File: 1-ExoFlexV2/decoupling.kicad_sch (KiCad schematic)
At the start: 158 parts

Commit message: Schématisation terminée
- Schéma terminé
- Passage vers le PCB
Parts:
- C100, C101, C110, C111, C112, C113, C114, C115, C116, C117, C125, C126, C127, C128, C129, C130, C131, C139, C140, C141, C142, C143, C144, C145, C153, C154, C155, C156, C157, C158, C159, C62, C63, C64, C65, C66, C67, C68, C69, C78, C79, C80, C81, C82, C83, C84, C85, C94, C95, C96, C97, C98, C99: renamed from C?; value 1uF -> 1uF 10V X6S; footprint Capacitor_SMD:C_0603_1608Metric -> Capacitor_SMD:C_0402_1005Metric; DESCRIPTION (none) -> 1 µF ±10% 10V Ceramic Capacitor X6S 0402 (1005 Metric); MANUFACTURER (none) -> Murata Electronics; PACKAGE (none) -> 0402 (1005 Metric); PART NUMBER (none) -> GRM155C81A105KA12D; TYPE (none) -> SMD
- C102, C103, C104, C105, C106, C107, C108, C109, C118, C119, C120, C121, C122, C123, C124, C132, C133, C134, C135, C136, C137, C138, C146, C147, C148, C149, C150, C151, C152, C160, C161, C162, C164, C165, C166, C167, C168, C169, C170, C171, C172, C173, C174, C175, C176, C177, C178, C179, C180, C181, C182, C183, C184, C185, C186, C187, C188, C189, C190, C191, C192, C193, C194, C195, C196, C197, C198, C199, C200, C201, C202, C203, C204, C205, C206, C207, C208, C209, C210, C211, C54, C55, C56, C57, C58, C59, C60, C61, C70, C71, C72, C73, C74, C75, C76, C77, C86, C87, C88, C89, C90, C91, C92, C93: renamed from C?; value 0,1uF -> 0,1uF 10V X5R; footprint Capacitor_SMD:C_0603_1608Metric -> Capacitor_SMD:C_0402_1005Metric; DESCRIPTION (none) -> 0.1 µF ±10% 10V Ceramic Capacitor X5R 0402 (1005 Metric); MANUFACTURER (none) -> Murata Electronics; PACKAGE (none) -> 0402 (1005 Metric); PART NUMBER (none) -> GRM155R61A104KA01D; TYPE (none) -> SMD
- C163: renamed from C?; value 0,1uF -> 0,1uF 10V X5R; footprint FootPrintLib:CAPC220145_88N_KEM -> Capacitor_SMD:C_0402_1005Metric; DESCRIPTION (none) -> 0.1 µF ±10% 10V Ceramic Capacitor X5R 0402 (1005 Metric); MANUFACTURER (none) -> Murata Electronics; PACKAGE (none) -> 0402 (1005 Metric); PART NUMBER (none) -> GRM155R61A104KA01D; TYPE (none) -> SMD

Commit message: PLACEMENT 1
- Placement des connnecteurs
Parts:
- added H1: MH1, MountingHole:MountingHole_2.2mm_M2, symbol Mechanical:MountingHole
- added H2: MH2, MountingHole:MountingHole_2.2mm_M2, symbol Mechanical:MountingHole
- added H3: MH3, MountingHole:MountingHole_2.2mm_M2, symbol Mechanical:MountingHole
- added H4: MH4, MountingHole:MountingHole_2.2mm_M2, symbol Mechanical:MountingHole
- added H5: MH5, MountingHole:MountingHole_2.2mm_M2, symbol Mechanical:MountingHole
- added H6: MH6, MountingHole:MountingHole_2.2mm_M2, symbol Mechanical:MountingHole
- added H7: MH7, MountingHole:MountingHole_2.2mm_M2, symbol Mechanical:MountingHole
- added H8: MH8, MountingHole:MountingHole_2.2mm_M2, symbol Mechanical:MountingHole
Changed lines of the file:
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@@
     (pin "2")
   )
+  (symbol (lib_id "Mechanical:MountingHole") (at 93.98 181.61 0) (unit 1)
+    (in_bom yes) (on_board yes)
+    (property "Reference" "H4" (id 0) (at 96.52 180.3399 0)
+      (effects (font (size 1.27 1.27)) (justify left))
+    )
+    (property "Value" "MH4" (id 1) (at 91.44 184.15 0)
+      (effects (font (size 1.27 1.27)) (justify left))
+    )
+    (property "Footprint" "MountingHole:MountingHole_2.2mm_M2" (id 2) (at 93.98 181.61 0)
+      (effects (font (size 1.27 1.27)) hide)
+    )
+    (property "Datasheet" "~" (id 3) (at 93.98 181.61 0)
+      (effects (font (size 1.27 1.27)) hide)
+    )
+  )
   (symbol (lib_id "Device:C") (at 214.63 132.08 0) (unit 1)
     (in_bom yes) (on_board yes)
@@
     (pin "2")
   )
+  (symbol (lib_id "Mechanical:MountingHole") (at 76.2 181.61 0) (unit 1)
+    (in_bom yes) (on_board yes)
+    (property "Reference" "H2" (id 0) (at 78.74 180.3399 0)
+      (effects (font (size 1.27 1.27)) (justify left))
+    )
+    (property "Value" "MH2" (id 1) (at 73.66 184.15 0)
+      (effects (font (size 1.27 1.27)) (justify left))
+    )
+    (property "Footprint" "MountingHole:MountingHole_2.2mm_M2" (id 2) (at 76.2 181.61 0)
+      (effects (font (size 1.27 1.27)) hide)
+    )
+    (property "Datasheet" "~" (id 3) (at 76.2 181.61 0)
+      (effects (font (size 1.27 1.27)) hide)
+    )
+  )
   (symbol (lib_id "Device:C") (at 223.52 54.61 0) (unit 1)
     (in_bom yes) (on_board yes)
@@
     (pin "2")
   )
+  (symbol (lib_id "Mechanical:MountingHole") (at 85.09 181.61 0) (unit 1)
+    (in_bom yes) (on_board yes)
+    (property "Reference" "H3" (id 0) (at 87.63 180.3399 0)
+      (effects (font (size 1.27 1.27)) (justify left))
+    )
+    (property "Value" "MH3" (id 1) (at 82.55 184.15 0)
+      (effects (font (size 1.27 1.27)) (justify left))
+    )
+    (property "Footprint" "MountingHole:MountingHole_2.2mm_M2" (id 2) (at 85.09 181.61 0)
+      (effects (font (size 1.27 1.27)) hide)
+    )
+    (property "Datasheet" "~" (id 3) (at 85.09 181.61 0)
+      (effects (font (size 1.27 1.27)) hide)
+    )
+  )
   (symbol (lib_id "Device:C") (at 259.08 54.61 0) (unit 1)
     (in_bom yes) (on_board yes)
@@
     (pin "2")
   )
+  (symbol (lib_id "Mechanical:MountingHole") (at 102.87 181.61 0) (unit 1)
+    (in_bom yes) (on_board yes)
+    (property "Reference" "H5" (id 0) (at 105.41 180.3399 0)
+      (effects (font (size 1.27 1.27)) (justify left))
+    )
+    (property "Value" "MH5" (id 1) (at 100.33 184.15 0)
+      (effects (font (size 1.27 1.27)) (justify left))
+    )
+    (property "Footprint" "MountingHole:MountingHole_2.2mm_M2" (id 2) (at 102.87 181.61 0)
+      (effects (font (size 1.27 1.27)) hide)
+    )
+    (property "Datasheet" "~" (id 3) (at 102.87 181.61 0)
+      (effects (font (size 1.27 1.27)) hide)
+    )
+  )
   (symbol (lib_id "Device:C") (at 86.36 55.88 0) (unit 1)
     (in_bom yes) (on_board yes)
@@
     (pin "2")
   )
+  (symbol (lib_id "Mechanical:MountingHole") (at 67.31 181.61 0) (unit 1)
+    (in_bom yes) (on_board yes)
+    (property "Reference" "H1" (id 0) (at 69.85 180.3399 0)
+      (effects (font (size 1.27 1.27)) (justify left))
+    )
+    (property "Value" "MH1" (id 1) (at 64.77 184.15 0)
+      (effects (font (size 1.27 1.27)) (justify left))
+    )
+    (property "Footprint" "MountingHole:MountingHole_2.2mm_M2" (id 2) (at 67.31 181.61 0)
+      (effects (font (size 1.27 1.27)) hide)
+    )
+    (property "Datasheet" "~" (id 3) (at 67.31 181.61 0)
+      (effects (font (size 1.27 1.27)) hide)
+    )
+  )
   (symbol (lib_id "Device:C") (at 147.32 41.91 0) (unit 1)
     (in_bom yes) (on_board yes)
@@
     (pin "2")
   )
+  (symbol (lib_id "Mechanical:MountingHole") (at 129.54 181.61 0) (unit 1)
+    (in_bom yes) (on_board yes)
+    (property "Reference" "H8" (id 0) (at 132.08 180.3399 0)
+      (effects (font (size 1.27 1.27)) (justify left))
+    )
+    (property "Value" "MH8" (id 1) (at 127 184.15 0)
+      (effects (font (size 1.27 1.27)) (justify left))
+    )
+    (property "Footprint" "MountingHole:MountingHole_2.2mm_M2" (id 2) (at 129.54 181.61 0)
+      (effects (font (size 1.27 1.27)) hide)
+    )
+    (property "Datasheet" "~" (id 3) (at 129.54 181.61 0)
+      (effects (font (size 1.27 1.27)) hide)
+    )
+  )
   (symbol (lib_id "Device:C") (at 250.19 67.31 0) (unit 1)
     (in_bom yes) (on_board yes)
@@
     (pin "2")
   )
+  (symbol (lib_id "Mechanical:MountingHole") (at 120.65 181.61 0) (unit 1)
+    (in_bom yes) (on_board yes)
+    (property "Reference" "H7" (id 0) (at 123.19 180.3399 0)
+      (effects (font (size 1.27 1.27)) (justify left))
+    )
+    (property "Value" "MH7" (id 1) (at 118.11 184.15 0)
+      (effects (font (size 1.27 1.27)) (justify left))
+    )
+    (property "Footprint" "MountingHole:MountingHole_2.2mm_M2" (id 2) (at 120.65 181.61 0)
+      (effects (font (size 1.27 1.27)) hide)
+    )
+    (property "Datasheet" "~" (id 3) (at 120.65 181.61 0)
+      (effects (font (size 1.27 1.27)) hide)
+    )
+  )
   (symbol (lib_id "Device:C") (at 50.8 133.35 0) (unit 1)
     (in_bom yes) (on_board yes)
@@
     (pin "2")
   )
+  (symbol (lib_id "Mechanical:MountingHole") (at 111.76 181.61 0) (unit 1)
+    (in_bom yes) (on_board yes)
+    (property "Reference" "H6" (id 0) (at 114.3 180.3399 0)
+      (effects (font (size 1.27 1.27)) (justify left))
+    )
+    (property "Value" "MH6" (id 1) (at 109.22 184.15 0)
+      (effects (font (size 1.27 1.27)) (justify left))
+    )
+    (property "Footprint" "MountingHole:MountingHole_2.2mm_M2" (id 2) (at 111.76 181.61 0)
+      (effects (font (size 1.27 1.27)) hide)
+    )
+    (property "Datasheet" "~" (id 3) (at 111.76 181.61 0)
+      (effects (font (size 1.27 1.27)) hide)
+    )
+  )
   (symbol (lib_id "Device:C") (at 187.96 93.98 0) (unit 1)

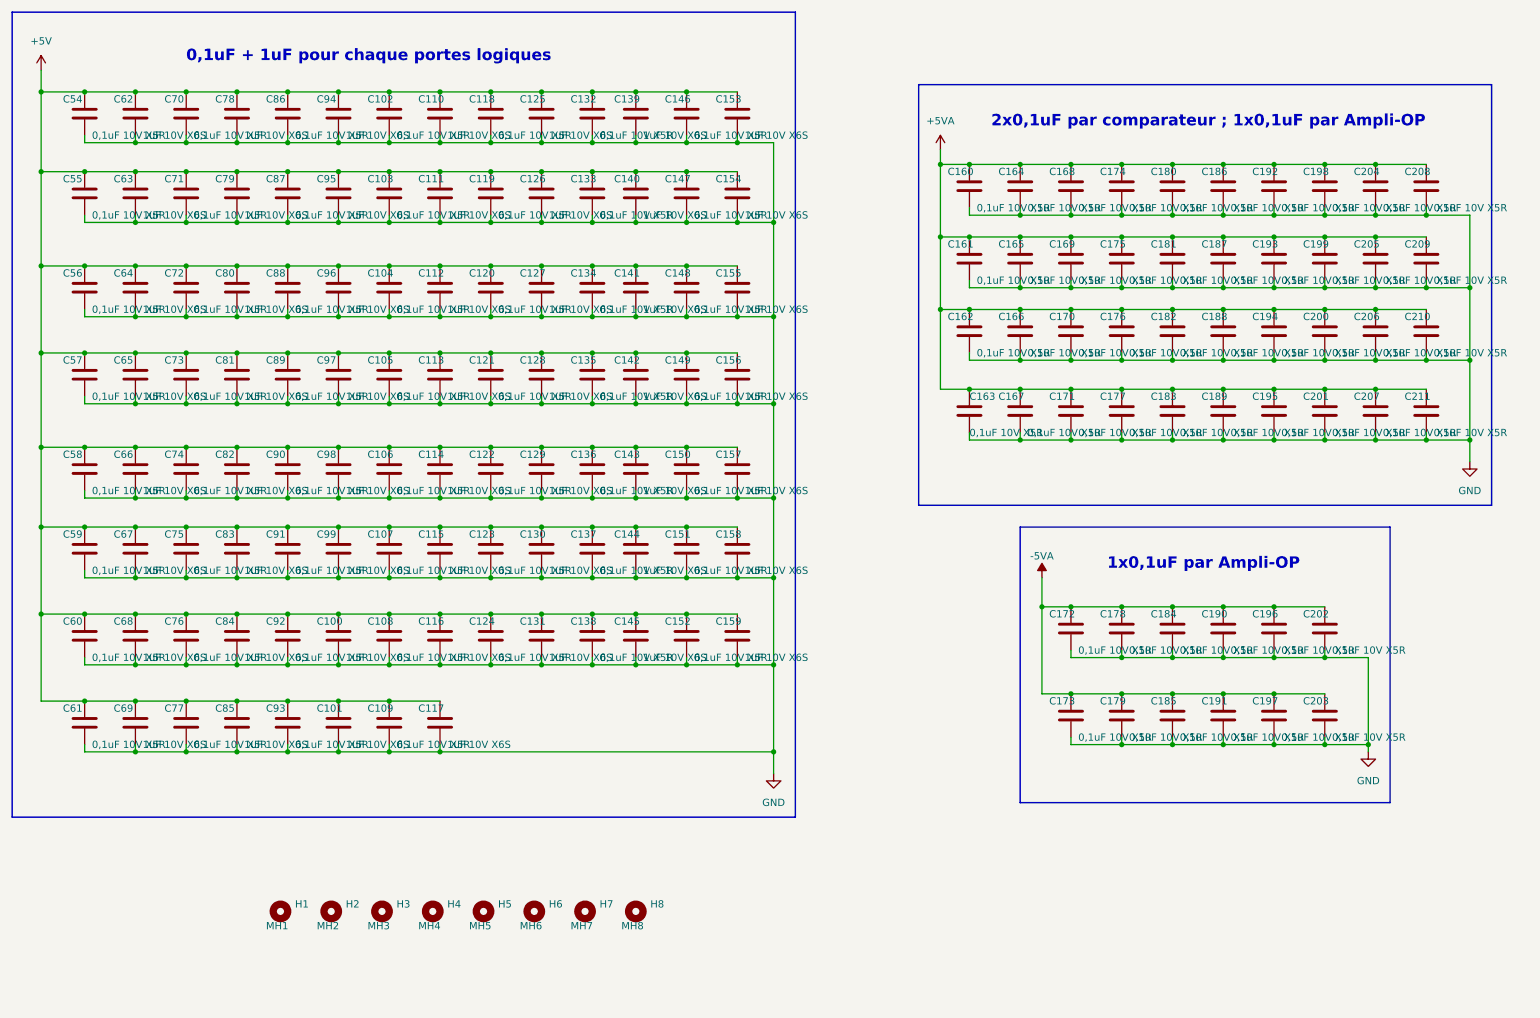
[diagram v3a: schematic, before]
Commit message: Finalisation 3
- Changement des régulateur de tension
- Retrait de test point inutile
- Changement de jumper mal positionner
- Ajout de Mounting holes et fiducial
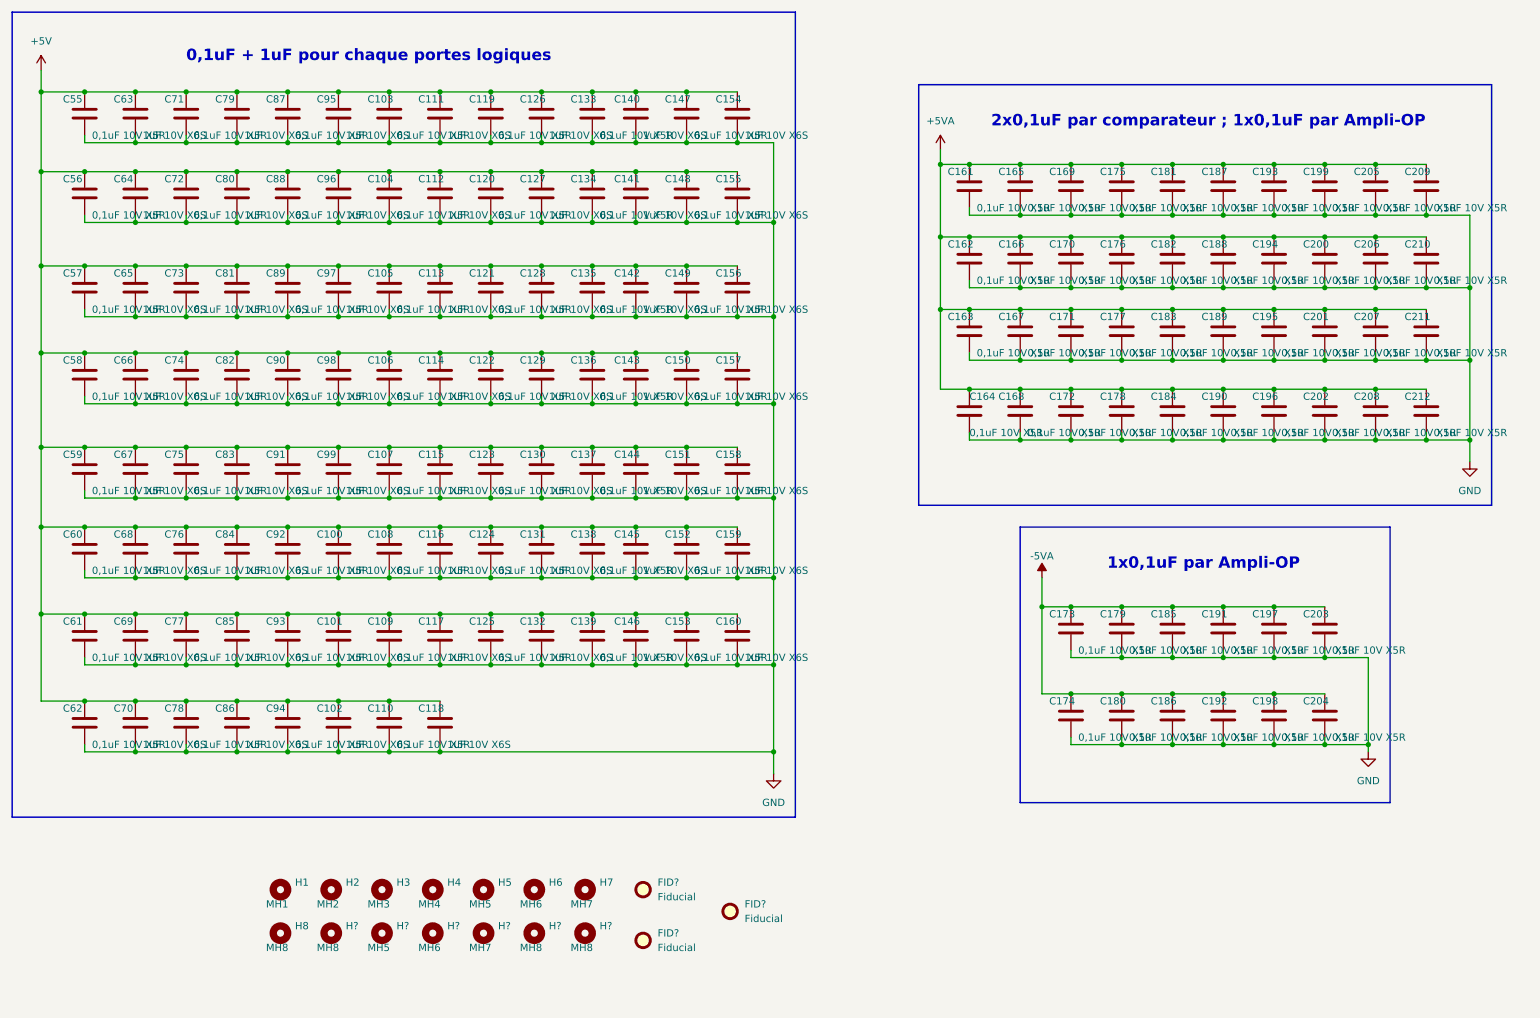
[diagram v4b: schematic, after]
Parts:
- added FID? (x3): Fiducial, symbol Mechanical:Fiducial
- added H? (x3): MH8, MountingHole:MountingHole_2.2mm_M2, symbol Mechanical:MountingHole
- added H?: MH7, MountingHole:MountingHole_2.2mm_M2, symbol Mechanical:MountingHole
- added H?: MH5, MountingHole:MountingHole_2.2mm_M2, symbol Mechanical:MountingHole
- added H?: MH6, MountingHole:MountingHole_2.2mm_M2, symbol Mechanical:MountingHole
- renumbered C99 to C100, C100 to C101, C101 to C102, C102 to C103, C103 to C104, C104 to C105, C105 to C106, C106 to C107, C107 to C108, C108 to C109, C109 to C110, C110 to C111, C111 to C112, C112 to C113, C113 to C114, C114 to C115, C115 to C116, C116 to C117, C117 to C118, C118 to C119, C119 to C120, C120 to C121, C121 to C122, C122 to C123, C123 to C124, C124 to C125, C125 to C126, C126 to C127, C127 to C128, C128 to C129, C129 to C130, C130 to C131, C131 to C132, C132 to C133, C133 to C134, C134 to C135, C135 to C136, C136 to C137, C137 to C138, C138 to C139, C139 to C140, C140 to C141, C141 to C142, C142 to C143, C143 to C144, C144 to C145, C145 to C146, C146 to C147, C147 to C148, C148 to C149, C149 to C150, C150 to C151, C151 to C152, C152 to C153, C153 to C154, C154 to C155, C155 to C156, C156 to C157, C157 to C158, C158 to C159, C159 to C160, C160 to C161, C161 to C162, C162 to C163, C163 to C164, C164 to C165, C165 to C166, C166 to C167, C167 to C168, C168 to C169, C169 to C170, C170 to C171, C171 to C172, C172 to C173, C173 to C174, C174 to C175, C175 to C176, C176 to C177, C177 to C178, C178 to C179, C179 to C180, C180 to C181, C181 to C182, C182 to C183, C183 to C184, C184 to C185, C185 to C186, C186 to C187, C187 to C188, C188 to C189, C189 to C190, C190 to C191, C191 to C192, C192 to C193, C193 to C194, C194 to C195, C195 to C196, C196 to C197, C197 to C198, C198 to C199, C199 to C200, C200 to C201, C201 to C202, C202 to C203, C203 to C204, C204 to C205, C205 to C206, C206 to C207, C207 to C208, C208 to C209, C209 to C210, C210 to C211, C211 to C212, C54 to C55, C55 to C56, C56 to C57, C57 to C58, C58 to C59, C59 to C60, C60 to C61, C61 to C62, C62 to C63, C63 to C64, C64 to C65, C65 to C66, C66 to C67, C67 to C68, C68 to C69, C69 to C70, C70 to C71, C71 to C72, C72 to C73, C73 to C74, C74 to C75, C75 to C76, C76 to C77, C77 to C78, C78 to C79, C79 to C80, C80 to C81, C81 to C82, C82 to C83, C83 to C84, C84 to C85, C85 to C86, C86 to C87, C87 to C88, C88 to C89, C89 to C90, C90 to C91, C91 to C92, C92 to C93, C93 to C94, C94 to C95, C95 to C96, C96 to C97, C97 to C98, C98 to C99
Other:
- moved on the sheet: H1, H2, H3, H4, H5, H6, H7, H8

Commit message: Finalisation schéma FIN
- Changement des uméro pour les inverseurs
- Changement des connecteur et début de placement
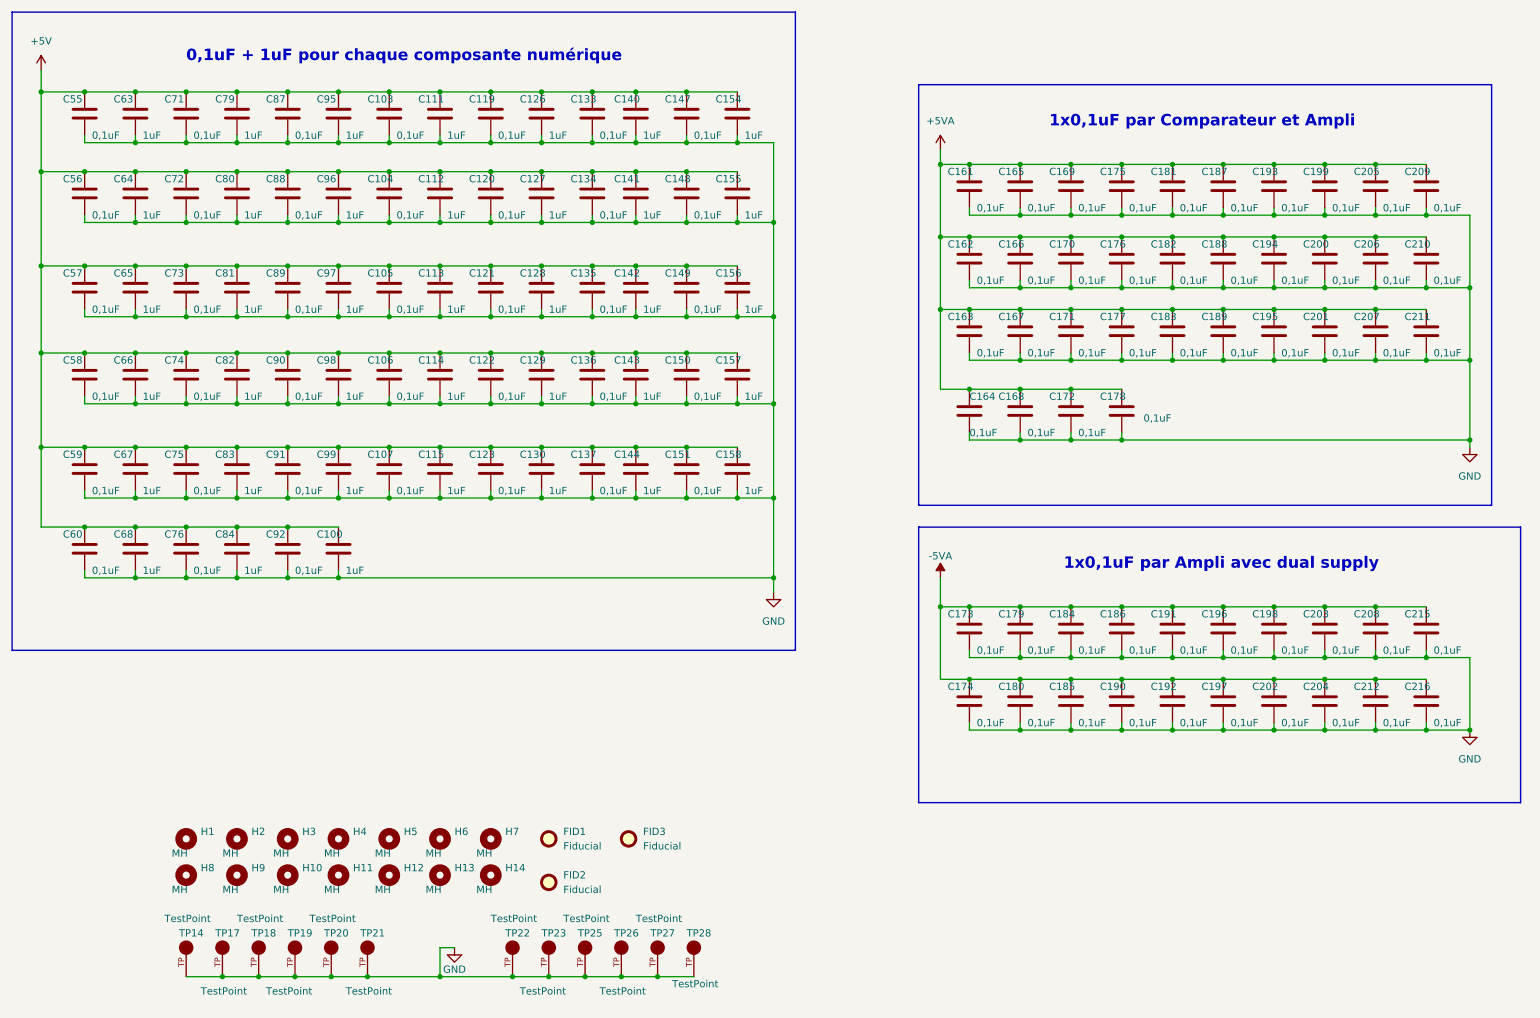
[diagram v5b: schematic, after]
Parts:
- removed C101, C102, C116, C117, C118, C131, C132, C145, C146, C159, C160, C69, C70, C85, C86: 1uF 10V X6S, Capacitor_SMD:C_0402_1005Metric, symbol Device:C
- removed C108, C109, C110, C124, C125, C138, C139, C152, C153, C61, C62, C77, C78, C93, C94: 0,1uF 10V X5R, Capacitor_SMD:C_0402_1005Metric, symbol Device:C
- added C215, C216: 0,1uF, Capacitor_SMD:C_0402_1005Metric, symbol Device:C
- added TP14, TP17, TP18, TP19, TP20, TP21, TP22, TP23, TP25, TP26, TP27, TP28: TestPoint, FootPrint:KEYSTONE_5005, symbol SymLib:5005
- C100, C111, C112, C113, C114, C115, C126, C127, C128, C129, C130, C140, C141, C142, C143, C144, C154, C155, C156, C157, C158, C63, C64, C65, C66, C67, C68, C79, C80, C81, C82, C83, C84, C95, C96, C97, C98, C99: value 1uF 10V X6S -> 1uF
- C103, C104, C105, C106, C107, C119, C120, C121, C122, C123, C133, C134, C135, C136, C137, C147, C148, C149, C150, C151, C161, C162, C163, C164, C165, C166, C167, C168, C169, C170, C171, C172, C173, C174, C175, C176, C177, C178, C179, C180, C181, C182, C183, C184, C185, C186, C187, C188, C189, C190, C191, C192, C193, C194, C195, C196, C197, C198, C199, C200, C201, C202, C203, C204, C205, C206, C207, C208, C209, C210, C211, C212, C55, C56, C57, C58, C59, C60, C71, C72, C73, C74, C75, C76, C87, C88, C89, C90, C91, C92: value 0,1uF 10V X5R -> 0,1uF
- FID1, FID2, FID3: renamed from FID?; footprint (none) -> Fiducial:Fiducial_0.5mm_Mask1.5mm
- H1: value MH1 -> MH
- H10: renamed from H?; value MH5 -> MH
- H11: renamed from H?; value MH6 -> MH
- H12: renamed from H?; value MH7 -> MH
- H13, H14, H9: renamed from H?; value MH8 -> MH
- H2: value MH2 -> MH
- H3: value MH3 -> MH
- H4: value MH4 -> MH
- H5: value MH5 -> MH
- H6: value MH6 -> MH
- H7: value MH7 -> MH
- H8: value MH8 -> MH
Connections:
- net +5VA: no longer C184.1, C190.1, C196.1, C202.1, C208.1, C212.1
- net -5VA: now also C184.1, C190.1, C196.1, C202.1, C208.1, C212.1, C215.1, C216.1
- net GND: now also C215.2, C216.2, TP14.TP, TP17.TP, TP18.TP, TP19.TP, TP20.TP, TP21.TP, TP22.TP, TP23.TP, TP25.TP, TP26.TP, TP27.TP, TP28.TP
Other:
- note added: "0,1uF + 1uF pour chaque composante numérique"
- note added: "1x0,1uF par Ampli avec dual supply"
- note added: "1x0,1uF par Comparateur et Ampli"
- note removed: "0,1uF + 1uF pour chaque portes logiques"
- note removed: "1x0,1uF par Ampli-OP"
- note removed: "2x0,1uF par comparateur ; 1x0,1uF par Ampli-OP"
- moved on the sheet: FID1, FID2, FID3, H1, H10, H11, H12, H13, H14, H2, H3, H4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

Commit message: PLacement 2
- Puissance
- signaux
-
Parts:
- removed TP22, TP23, TP25, TP26, TP27, TP28: TestPoint, FootPrint:KEYSTONE_5005, symbol SymLib:5005
